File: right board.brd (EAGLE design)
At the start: 100 x 80 mm, 50 parts, among them IC1 LM555D, IC2 LM555D, Q1 10, Q2 10

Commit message: all gerbers generated
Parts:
- added H1, H2, H3, H4: STAND-OFF, SparkFun-Electromechanical:STAND-OFF
- moved R_DRIVE 7.62 mm to (101.6, 17.8)
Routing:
- net DRIVE: track 7.98 -> 10.5 mm
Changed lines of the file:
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@@
 </element>
 <element name="R_BLINK" library="TE 2-pin connector" package="2_PIN_CONNECT" value="2_PIN_TECONNECTOR" x="101.6" y="36.83" rot="R90"/>
-<element name="R_DRIVE" library="TE 2-pin connector" package="2_PIN_CONNECT" value="2_PIN_TECONNECTOR" x="101.6" y="10.16" rot="R90"/>
+<element name="R_DRIVE" library="TE 2-pin connector" package="2_PIN_CONNECT" value="2_PIN_TECONNECTOR" x="101.6" y="17.78" rot="R90"/>
 <element name="U$1" library="slide switch" package="MYPART3" value="JS_SERIES_SLIDESWITCCH" x="81.28" y="33.02" rot="R90"/>
 <element name="U$2" library="slide switch" package="MYPART3" value="JS_SERIES_SLIDESWITCCH" x="81.28" y="7.62" rot="R90"/>
@@
 <attribute name="PROD_ID" value="RES-12428" x="27.94" y="3.81" size="1.778" layer="28" rot="MR0" display="off"/>
 </element>
+<element name="H1" library="SparkFun-Electromechanical" package="STAND-OFF" value="STAND-OFF" x="5.08" y="5.08"/>
+<element name="H2" library="SparkFun-Electromechanical" package="STAND-OFF" value="STAND-OFF" x="5.08" y="74.93"/>
+<element name="H3" library="SparkFun-Electromechanical" package="STAND-OFF" value="STAND-OFF" x="93.98" y="74.93"/>
+<element name="H4" library="SparkFun-Electromechanical" package="STAND-OFF" value="STAND-OFF" x="95.25" y="5.08"/>
 </elements>
 <signals>
@@
 <contactref element="R_DRIVE" pad="V/SIG"/>
 <contactref element="U$2" pad="IN"/>
-<wire x1="88.93" y1="6.82" x2="82.08" y2="6.82" width="0.4064" layer="16"/>
-<wire x1="82.08" y1="6.82" x2="81.28" y2="7.62" width="0.4064" layer="16"/>
+<wire x1="81.28" y1="7.62" x2="82.11" y2="7.62" width="0.6096" layer="1"/>
+<wire x1="82.11" y1="7.62" x2="88.93" y2="14.44" width="0.6096" layer="1"/>
 </signal>
 <signal name="B_OUT">

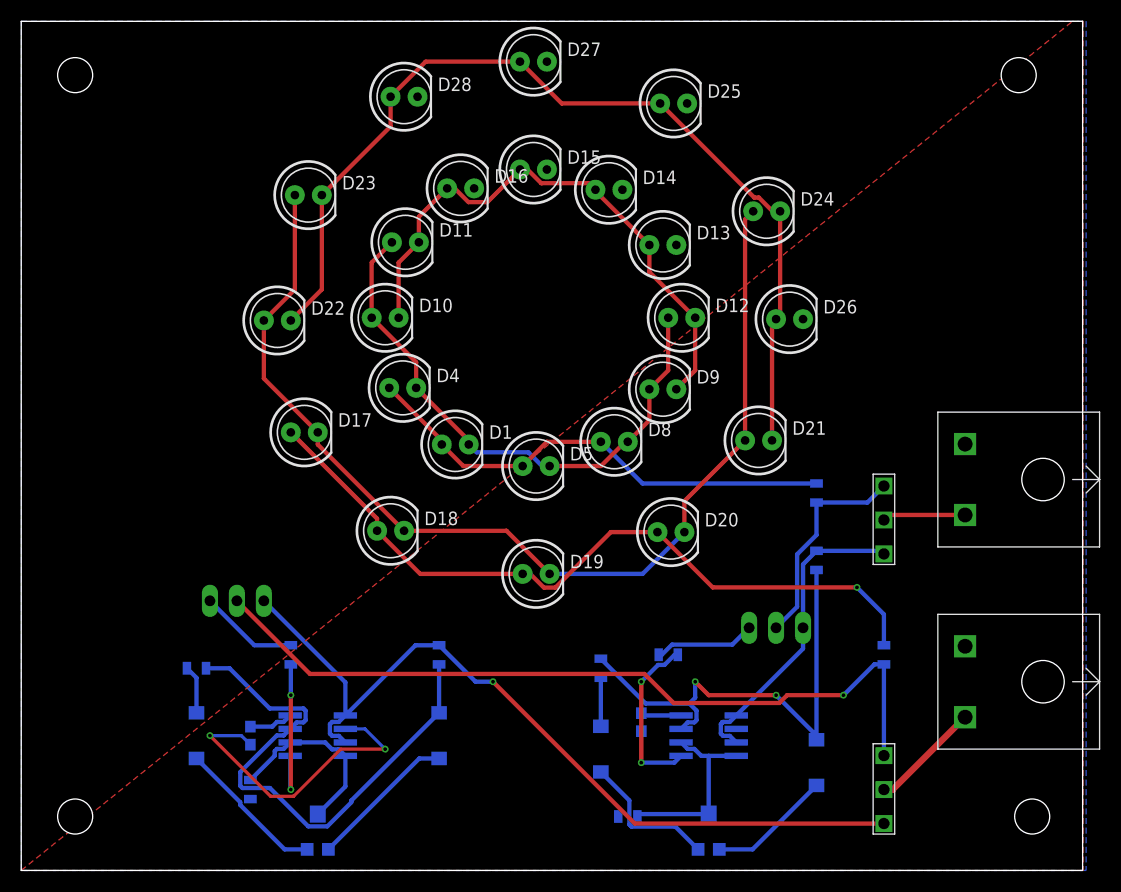
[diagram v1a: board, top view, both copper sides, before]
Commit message: added reverse polairity protection
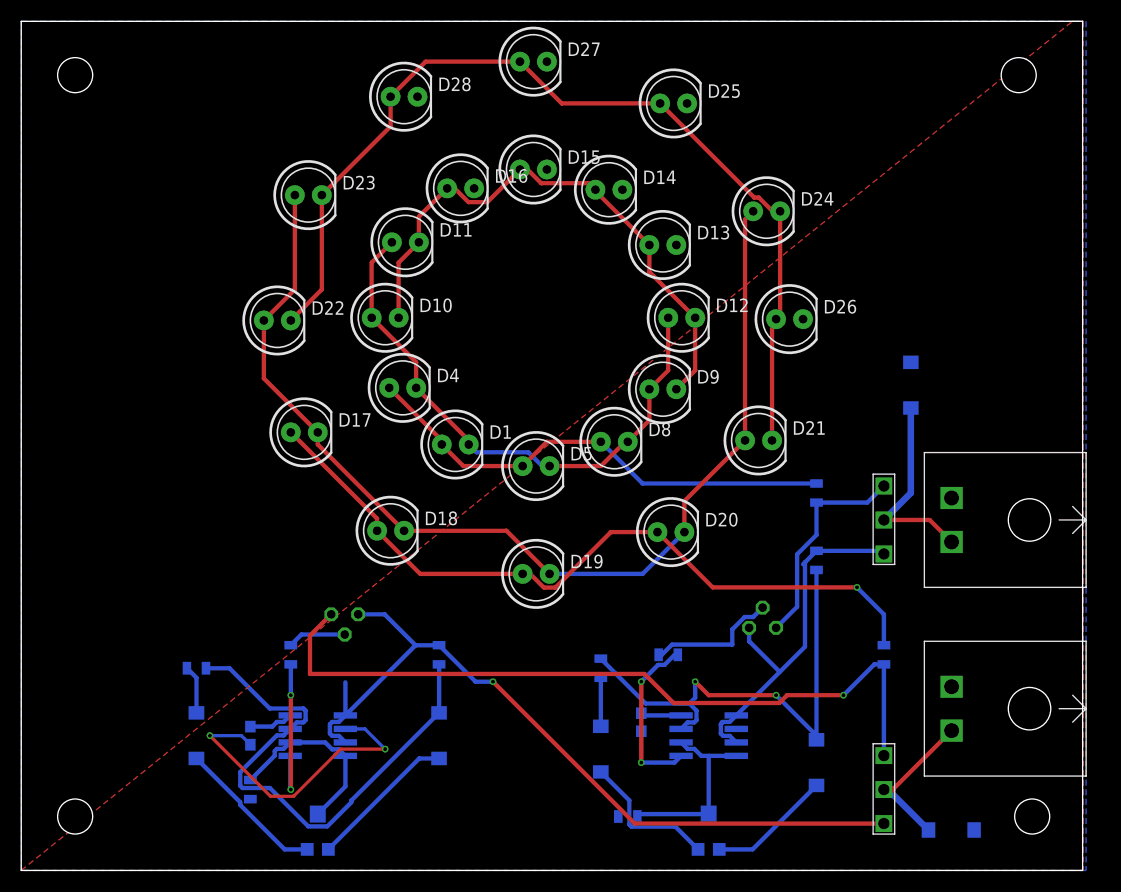
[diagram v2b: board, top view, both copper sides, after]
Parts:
- removed Q2: 10, transistor-power:TO220BV
- removed R_BLINK, R_DRIVE: 2_PIN_TECONNECTOR, TE 2-pin connector:2_PIN_CONNECT
- added D2, D3: MBRA140, SparkFun-DiscreteSemi:SMA-DIODE
- added Q3: BSS101, transistor-fet:TO92
- added U$5, U$6: 2_PIN_TECONNECTOR, TE 2-pin connector:2_PIN_CONNECT
- Q1: value 10 -> BSS101; device transistor-power:TO220BV -> transistor-fet:TO92
- moved Q1 49.5 mm to (69.8, 22.9), turned to 0 degrees
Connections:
- net BLINK: now also D3.C, U$5.V/SIG; no longer R_BLINK.V/SIG
- net B_BLINK: now also Q1.1; no longer Q2.S
- net B_OUT: now also Q1.3; no longer Q2.D
- net DRIVE: now also D2.C, U$6.V/SIG; no longer R_DRIVE.V/SIG
- net D_BLINK: now also Q3.1; no longer Q1.S
- net D_OUT: now also Q3.3; no longer Q1.D
- net GND: now also D2.A, D3.A, U$5.G/LOW, U$6.G/LOW; no longer R_BLINK.G/LOW, R_DRIVE.G/LOW
- net N$19: now also Q3.2; no longer Q1.G
- net N$8: now also Q1.2; no longer Q2.G
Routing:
- net BLINK: track 7.84 -> 19.5 mm
- net B_BLINK: track 29.6 -> 35.2 mm
- net D_BLINK: track 78.9 -> 74.7 mm
- net DRIVE: track 10.5 -> 14.5 mm
- net N$19: track 9.35 -> 5.50 mm
- net D_OUT: track 75.1 -> 71.8 mm
- net N$8: track 9.57 -> 12.5 mm
